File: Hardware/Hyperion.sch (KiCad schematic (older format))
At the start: 0 parts

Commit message: Rough USB interface
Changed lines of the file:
@@
 LIBS:power
 LIBS:Aerodyne_v2
+LIBS:Hyperion-cache
 EELAYER 27 0
 EELAYER END
@@
 Sheet 1 3
 Title ""
-Date "26 feb 2014"
+Date "28 feb 2014"
 Rev ""
 Comp ""
@@
 F0 "Interface Port" 50
 F1 "Interface-Port.sch" 50
+F2 "TCK" O R 2800 3300 60
+F3 "TDI" O R 2800 3400 60
+F4 "TDO" I R 2800 3500 60
+F5 "TMS" O R 2800 3600 60
+F6 "TXD" O R 2800 3900 60
+F7 "RXD" I R 2800 4000 60
+F8 "RST" O R 2800 3700 60
 $EndSheet
 $EndSCHEMATC

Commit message: Core support circuitry
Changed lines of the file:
@@
 $Descr A4 11693 8268
 encoding utf-8
-Sheet 1 3
+Sheet 1 4
 Title ""
-Date "4 mar 2014"
+Date "12 mar 2014"
 Rev ""
 Comp ""
@@
 F8 "RST" O R 2800 3700 60
 $EndSheet
+$Sheet
+S 3800 1200 1000 2000
+U 531F27A0
+F0 "Core" 50
+F1 "Core.sch" 50
+F2 "TDI" I L 3800 1400 60
+F3 "TDO" O L 3800 1500 60
+F4 "TCK" I L 3800 1300 60
+F5 "TMS" I L 3800 1600 60
+$EndSheet
+Wire Wire Line
+	2800 3300 2900 3300
+Wire Wire Line
+	2900 3300 2900 1300
+Wire Wire Line
+	2900 1300 3800 1300
+Wire Wire Line
+	2800 3400 3000 3400
+Wire Wire Line
+	3000 3400 3000 1400
+Wire Wire Line
+	3000 1400 3800 1400
+Wire Wire Line
+	2800 3500 3100 3500
+Wire Wire Line
+	3100 3500 3100 1500
+Wire Wire Line
+	3100 1500 3800 1500
+Wire Wire Line
+	2800 3600 3200 3600
+Wire Wire Line
+	3200 3600 3200 1600
+Wire Wire Line
+	3200 1600 3800 1600
 $EndSCHEMATC

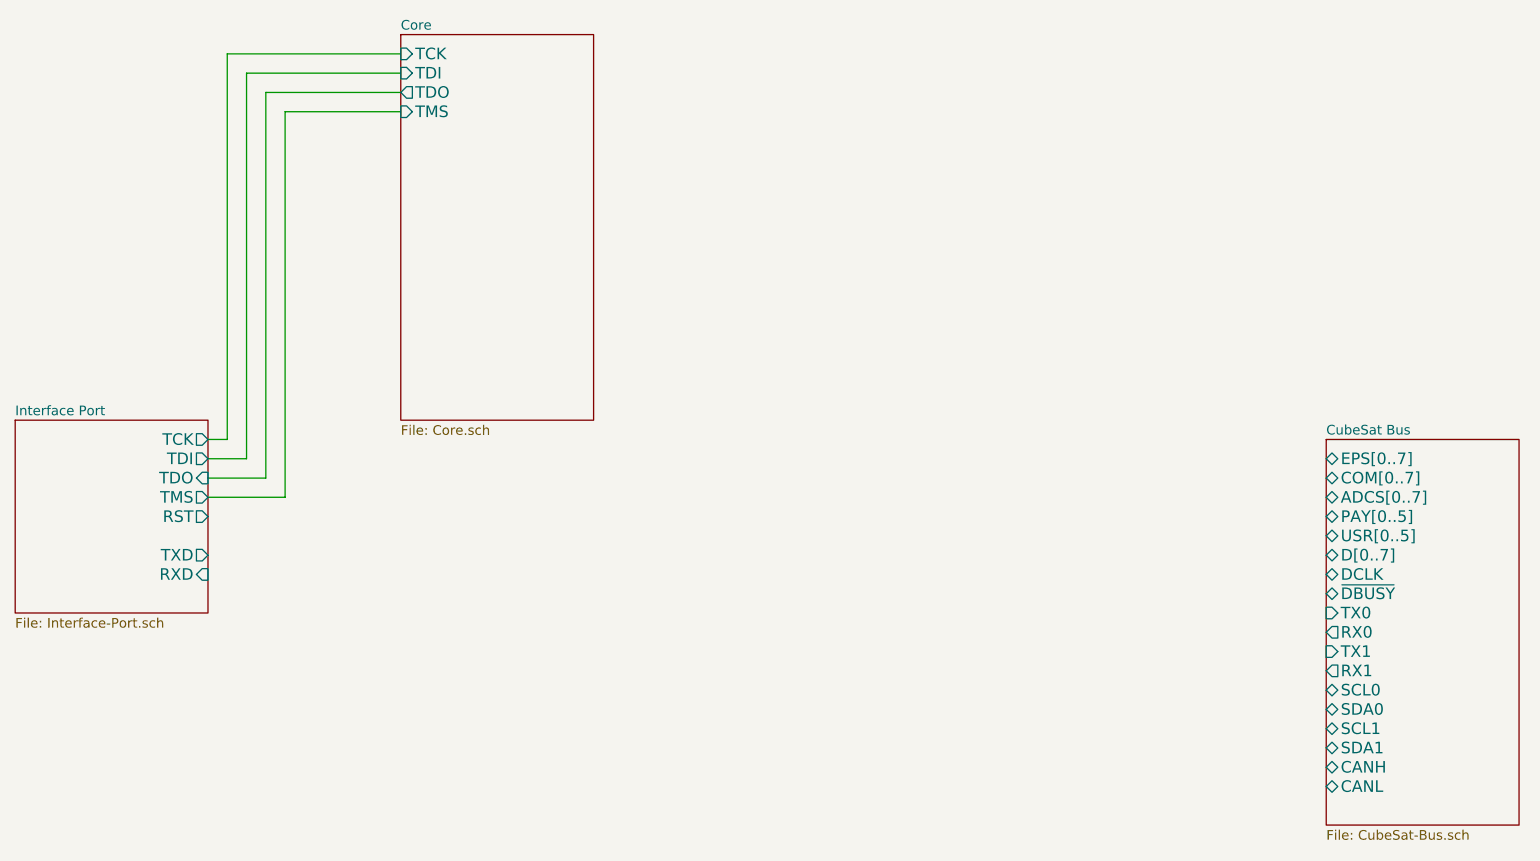
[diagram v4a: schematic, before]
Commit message: Testing bottom side decoupling
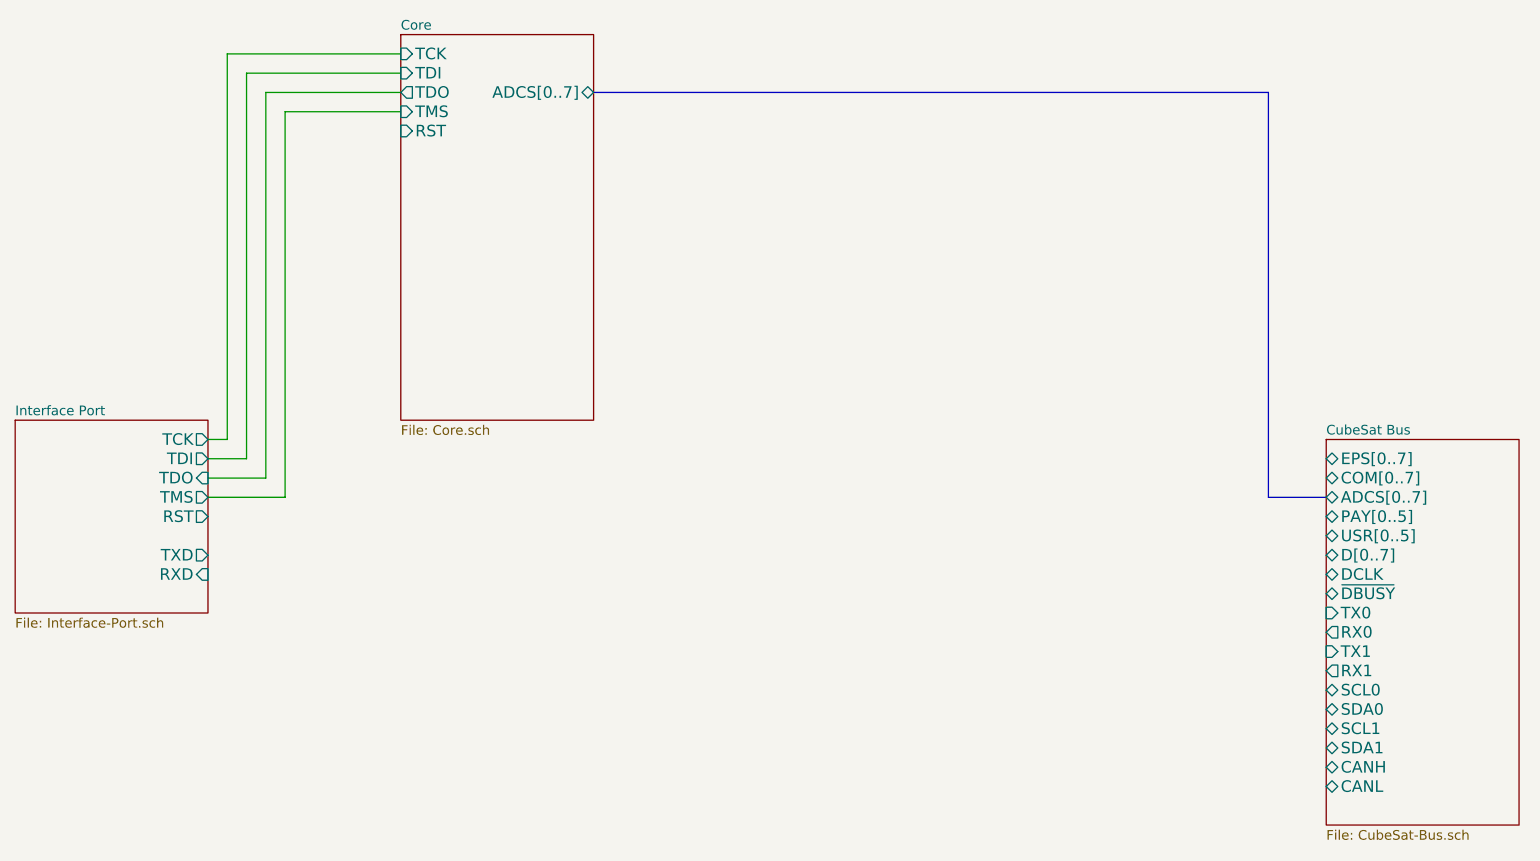
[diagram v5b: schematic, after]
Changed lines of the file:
@@
 Sheet 1 4
 Title ""
-Date "12 mar 2014"
+Date "15 mar 2014"
 Rev ""
 Comp ""
@@
 F4 "TCK" I L 3800 1300 60
 F5 "TMS" I L 3800 1600 60
+F6 "RST" I L 3800 1700 60
+F7 "ADCS[0..7]" B R 4800 1500 60
 $EndSheet
 Wire Wire Line
@@
 Wire Wire Line
 	3200 1600 3800 1600
+Wire Bus Line
+	4800 1500 8300 1500
+Wire Bus Line
+	8300 1500 8300 3600
+Wire Bus Line
+	8300 3600 8600 3600
 $EndSCHEMATC

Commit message: Add CAN transceiver
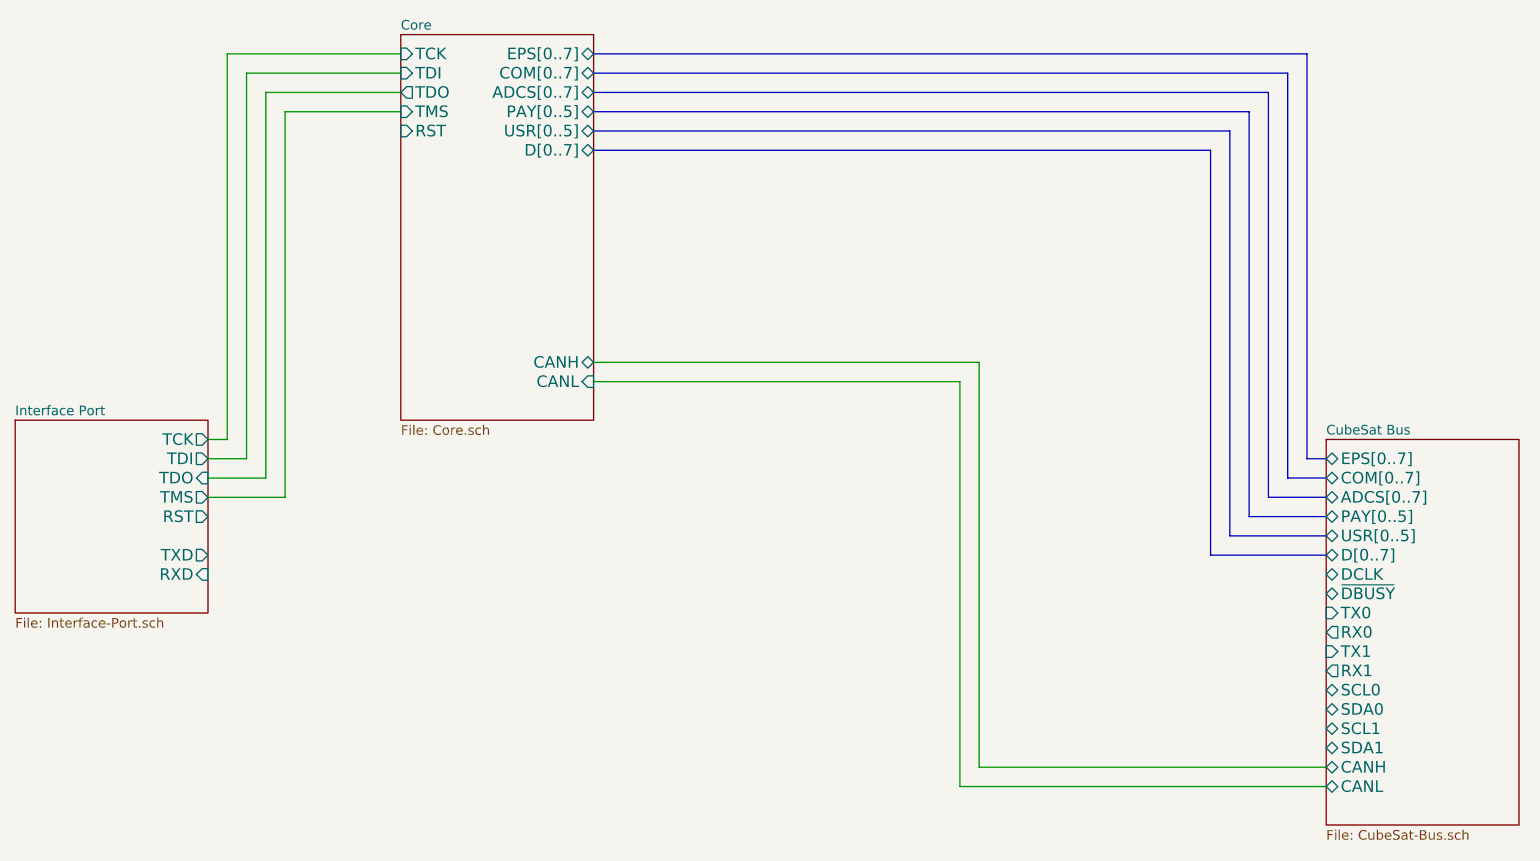
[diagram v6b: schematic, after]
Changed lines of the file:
@@
 Sheet 1 4
 Title ""
-Date "15 mar 2014"
+Date "16 mar 2014"
 Rev ""
 Comp ""
@@
 F6 "RST" I L 3800 1700 60
 F7 "ADCS[0..7]" B R 4800 1500 60
+F8 "EPS[0..7]" B R 4800 1300 60
+F9 "COM[0..7]" B R 4800 1400 60
+F10 "PAY[0..5]" B R 4800 1600 60
+F11 "USR[0..5]" B R 4800 1700 60
+F12 "D[0..7]" B R 4800 1800 60
+F13 "CANH" B R 4800 2900 60
+F14 "CANL" I R 4800 3000 60
 $EndSheet
 Wire Wire Line
@@
 Wire Bus Line
 	8300 3600 8600 3600
+Wire Bus Line
+	4800 1400 8400 1400
+Wire Bus Line
+	8400 1400 8400 3500
+Wire Bus Line
+	8400 3500 8600 3500
+Wire Bus Line
+	8600 3400 8500 3400
+Wire Bus Line
+	8500 3400 8500 1300
+Wire Bus Line
+	8500 1300 4800 1300
+Wire Bus Line
+	4800 1600 8200 1600
+Wire Bus Line
+	8200 1600 8200 3700
+Wire Bus Line
+	8200 3700 8600 3700
+Wire Bus Line
+	8600 3800 8100 3800
+Wire Bus Line
+	8100 3800 8100 1700
+Wire Bus Line
+	8100 1700 4800 1700
+Wire Bus Line
+	4800 1800 8000 1800
+Wire Bus Line
+	8000 1800 8000 3900
+Wire Bus Line
+	8000 3900 8600 3900
+Wire Wire Line
+	4800 3000 6700 3000
+Wire Wire Line
+	6700 3000 6700 5100
+Wire Wire Line
+	6700 5100 8600 5100
+Wire Wire Line
+	8600 5000 6800 5000
+Wire Wire Line
+	6800 5000 6800 2900
+Wire Wire Line
+	6800 2900 4800 2900
 $EndSCHEMATC

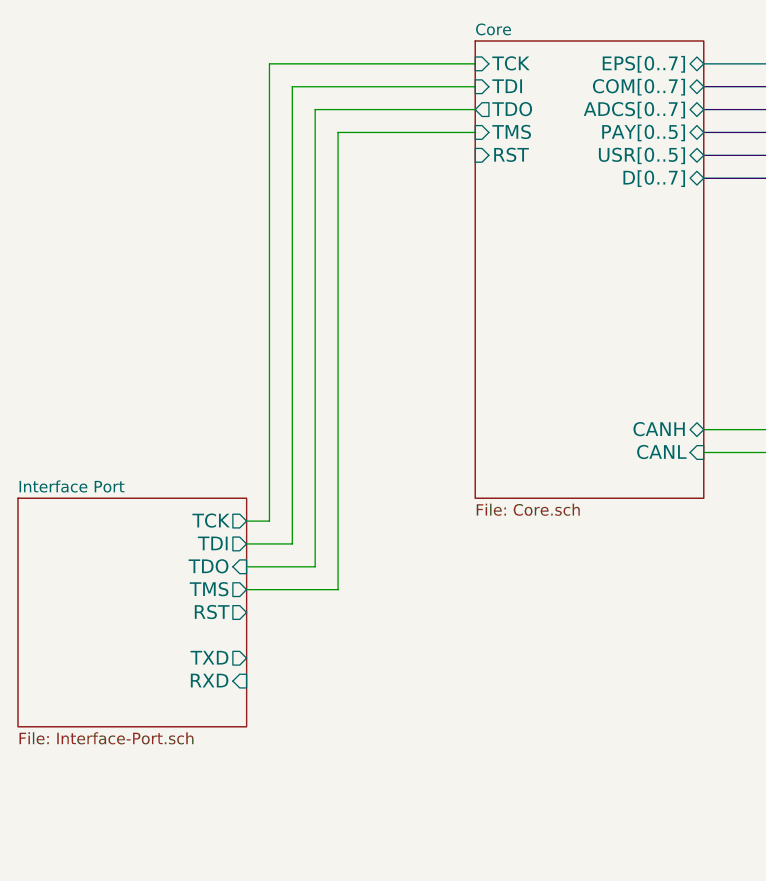
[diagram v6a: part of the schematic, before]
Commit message: Switch to STM32F4 MCU
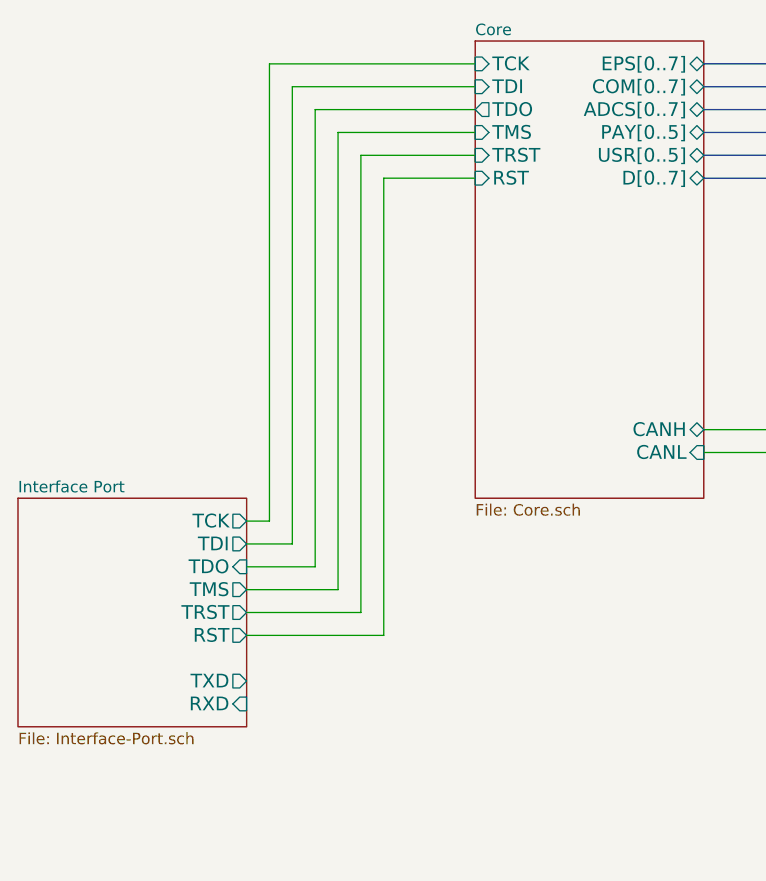
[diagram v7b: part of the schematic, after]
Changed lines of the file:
@@
 Sheet 1 4
 Title ""
-Date "16 mar 2014"
+Date "17 mar 2014"
 Rev ""
 Comp ""
@@
 F4 "TDO" I R 2800 3500 60
 F5 "TMS" O R 2800 3600 60
-F6 "TXD" O R 2800 3900 60
-F7 "RXD" I R 2800 4000 60
-F8 "RST" O R 2800 3700 60
+F6 "TXD" O R 2800 4000 60
+F7 "RXD" I R 2800 4100 60
+F8 "RST" O R 2800 3800 60
+F9 "TRST" O R 2800 3700 60
 $EndSheet
 $Sheet
@@
 F4 "TCK" I L 3800 1300 60
 F5 "TMS" I L 3800 1600 60
-F6 "RST" I L 3800 1700 60
+F6 "RST" I L 3800 1800 60
 F7 "ADCS[0..7]" B R 4800 1500 60
 F8 "EPS[0..7]" B R 4800 1300 60
@@
 F13 "CANH" B R 4800 2900 60
 F14 "CANL" I R 4800 3000 60
+F15 "TRST" I L 3800 1700 60
 $EndSheet
 Wire Wire Line
@@
 Wire Wire Line
 	6800 2900 4800 2900
+Wire Wire Line
+	2800 3700 3300 3700
+Wire Wire Line
+	3300 3700 3300 1700
+Wire Wire Line
+	3300 1700 3800 1700
+Wire Wire Line
+	2800 3800 3400 3800
+Wire Wire Line
+	3400 3800 3400 1800
+Wire Wire Line
+	3400 1800 3800 1800
 $EndSCHEMATC

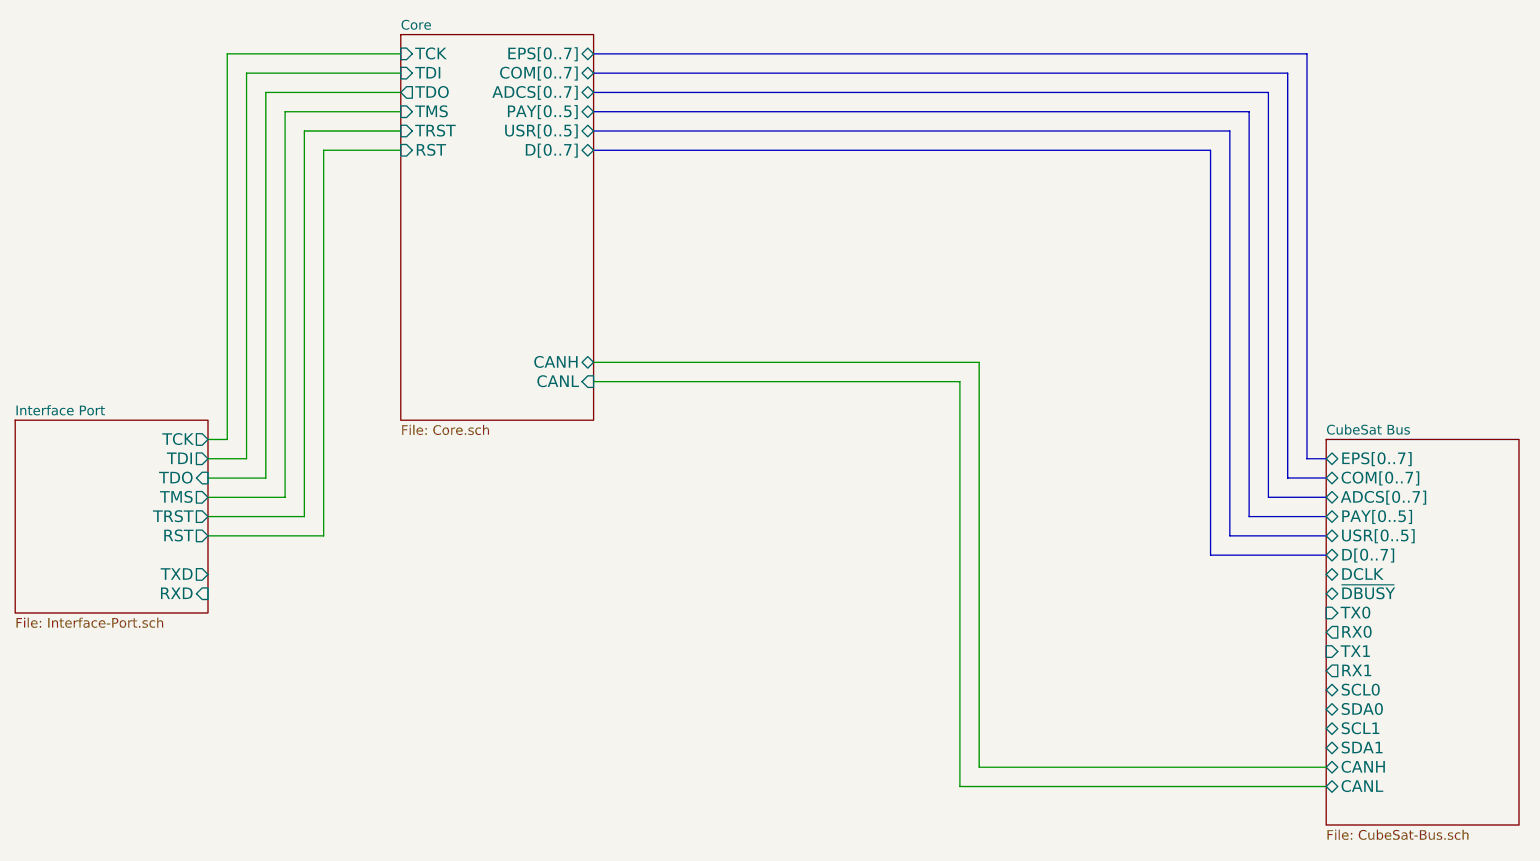
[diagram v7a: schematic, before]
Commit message: Clear core in prep for new MCU
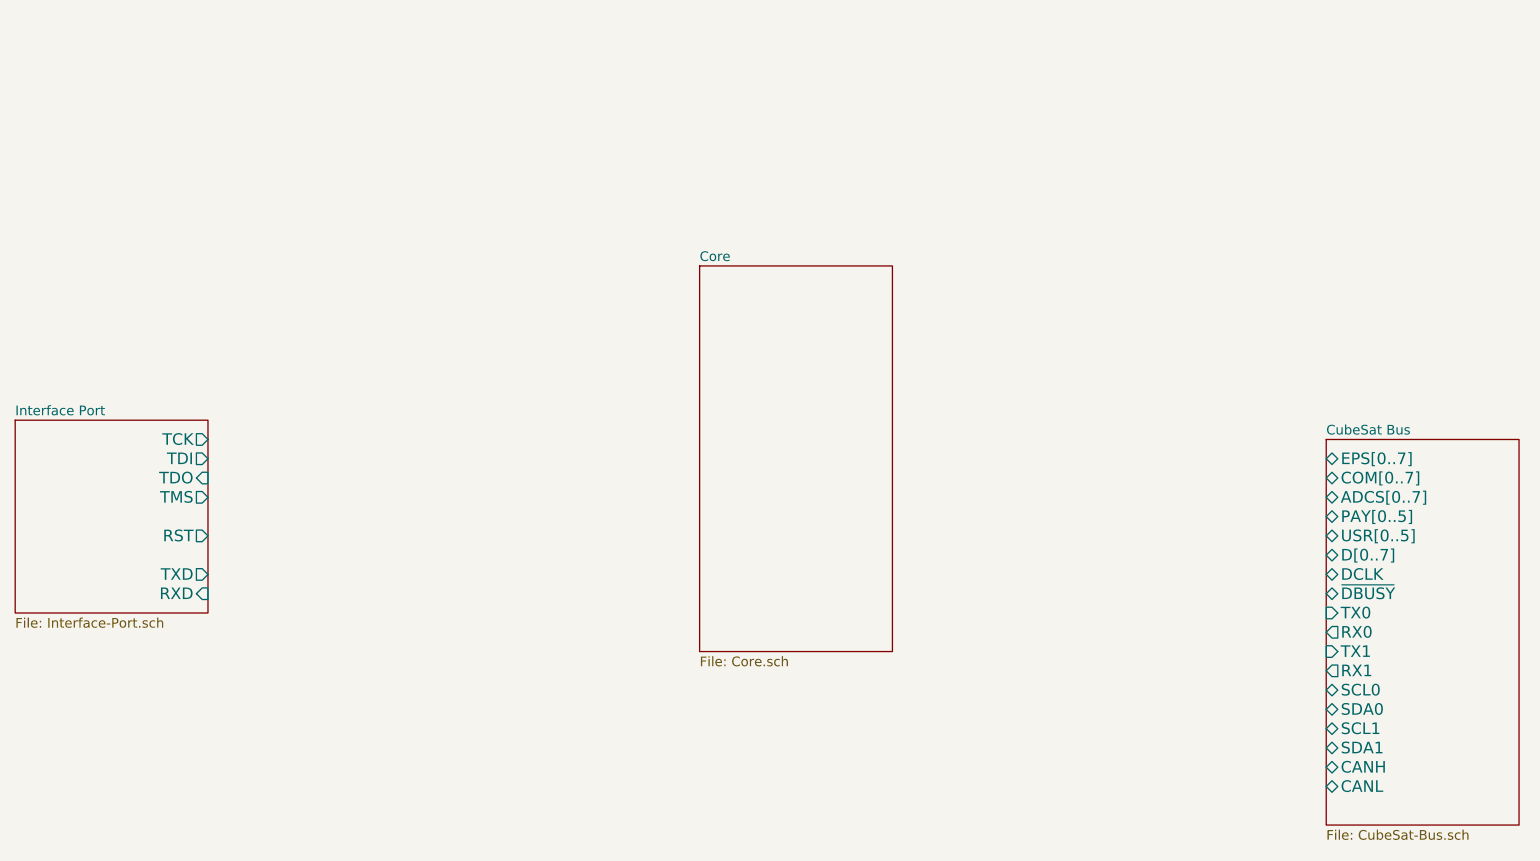
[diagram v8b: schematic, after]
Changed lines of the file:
@@
 encoding utf-8
 Sheet 1 4
-Title ""
-Date "17 mar 2014"
-Rev ""
-Comp ""
-Comment1 ""
+Title "Hyperion"
+Date "1 apr 2014"
+Rev "0.2"
+Comp "Aerodyne Labs"
+Comment1 "ethanharstad@gmail.com"
 Comment2 ""
 Comment3 ""
@@
 F7 "RXD" I R 2800 4100 60
 F8 "RST" O R 2800 3800 60
-F9 "TRST" O R 2800 3700 60
 $EndSheet
 $Sheet
-S 3800 1200 1000 2000
-U 531F27A0
+S 5350 2400 1000 2000
+U 533BABFA
 F0 "Core" 50
 F1 "Core.sch" 50
-F2 "TDI" I L 3800 1400 60
-F3 "TDO" O L 3800 1500 60
-F4 "TCK" I L 3800 1300 60
-F5 "TMS" I L 3800 1600 60
-F6 "RST" I L 3800 1800 60
-F7 "ADCS[0..7]" B R 4800 1500 60
-F8 "EPS[0..7]" B R 4800 1300 60
-F9 "COM[0..7]" B R 4800 1400 60
-F10 "PAY[0..5]" B R 4800 1600 60
-F11 "USR[0..5]" B R 4800 1700 60
-F12 "D[0..7]" B R 4800 1800 60
-F13 "CANH" B R 4800 2900 60
-F14 "CANL" I R 4800 3000 60
-F15 "TRST" I L 3800 1700 60
 $EndSheet
-Wire Wire Line
-	2800 3300 2900 3300
-Wire Wire Line
-	2900 3300 2900 1300
-Wire Wire Line
-	2900 1300 3800 1300
-Wire Wire Line
-	2800 3400 3000 3400
-Wire Wire Line
-	3000 3400 3000 1400
-Wire Wire Line
-	3000 1400 3800 1400
-Wire Wire Line
-	2800 3500 3100 3500
-Wire Wire Line
-	3100 3500 3100 1500
-Wire Wire Line
-	3100 1500 3800 1500
-Wire Wire Line
-	2800 3600 3200 3600
-Wire Wire Line
-	3200 3600 3200 1600
-Wire Wire Line
-	3200 1600 3800 1600
-Wire Bus Line
-	4800 1500 8300 1500
-Wire Bus Line
-	8300 1500 8300 3600
-Wire Bus Line
-	8300 3600 8600 3600
-Wire Bus Line
-	4800 1400 8400 1400
-Wire Bus Line
-	8400 1400 8400 3500
-Wire Bus Line
-	8400 3500 8600 3500
-Wire Bus Line
-	8600 3400 8500 3400
-Wire Bus Line
-	8500 3400 8500 1300
-Wire Bus Line
-	8500 1300 4800 1300
-Wire Bus Line
-	4800 1600 8200 1600
-Wire Bus Line
-	8200 1600 8200 3700
-Wire Bus Line
-	8200 3700 8600 3700
-Wire Bus Line
-	8600 3800 8100 3800
-Wire Bus Line
-	8100 3800 8100 1700
-Wire Bus Line
-	8100 1700 4800 1700
-Wire Bus Line
-	4800 1800 8000 1800
-Wire Bus Line
-	8000 1800 8000 3900
-Wire Bus Line
-	8000 3900 8600 3900
-Wire Wire Line
-	4800 3000 6700 3000
-Wire Wire Line
-	6700 3000 6700 5100
-Wire Wire Line
-	6700 5100 8600 5100
-Wire Wire Line
-	8600 5000 6800 5000
-Wire Wire Line
-	6800 5000 6800 2900
-Wire Wire Line
-	6800 2900 4800 2900
-Wire Wire Line
-	2800 3700 3300 3700
-Wire Wire Line
-	3300 3700 3300 1700
-Wire Wire Line
-	3300 1700 3800 1700
-Wire Wire Line
-	2800 3800 3400 3800
-Wire Wire Line
-	3400 3800 3400 1800
-Wire Wire Line
-	3400 1800 3800 1800
 $EndSCHEMATC
